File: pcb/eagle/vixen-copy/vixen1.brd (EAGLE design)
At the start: 89.6 x 59.5 mm, 33 parts, among them CN1 EXPANSIONPORT-VIC20-EDGEEDGE, IC1 74HCT393N, IC2 74AC157N, IC3 74AC157N, IC4 74AC157N, IC5 74AC157N, IC6 74ALS11N, IC8 74132N, IC9 74LS00N, U1 TMS4416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

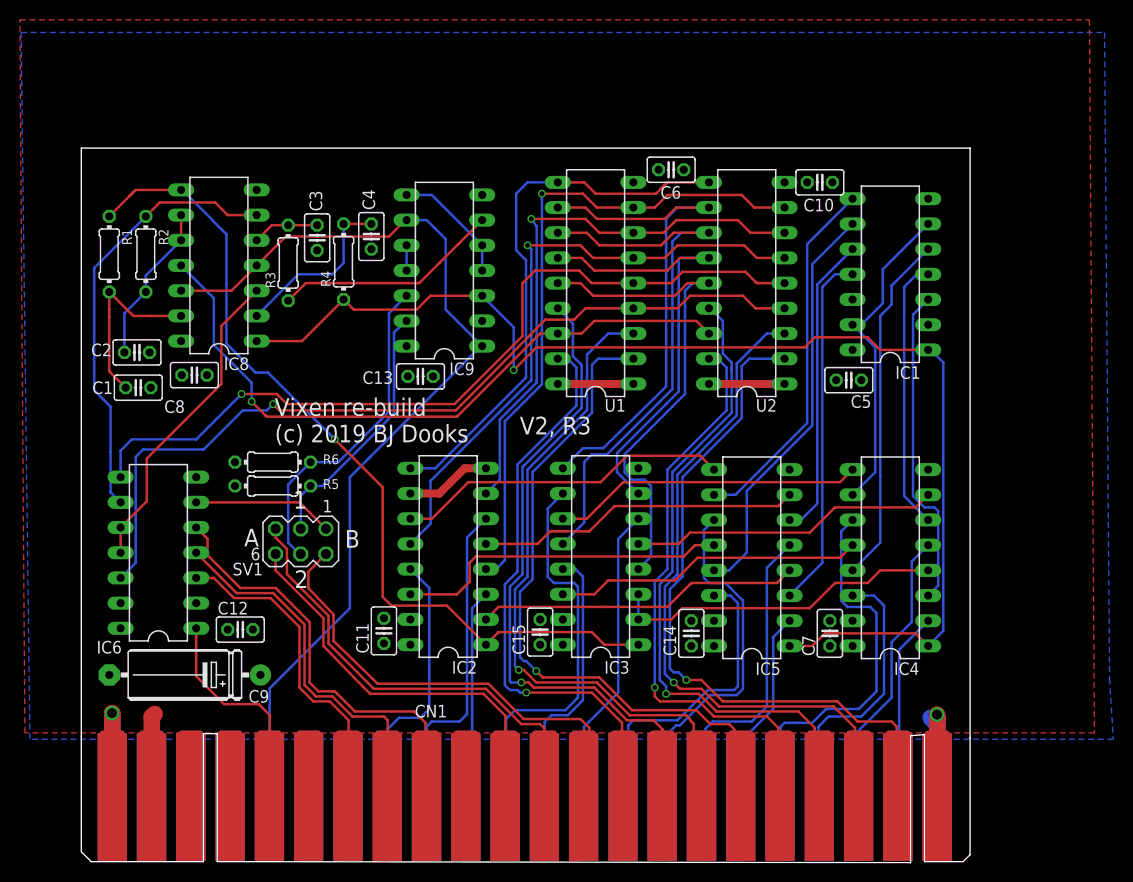
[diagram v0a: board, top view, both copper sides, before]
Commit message: vixen: minor pcb updates for v2,r3
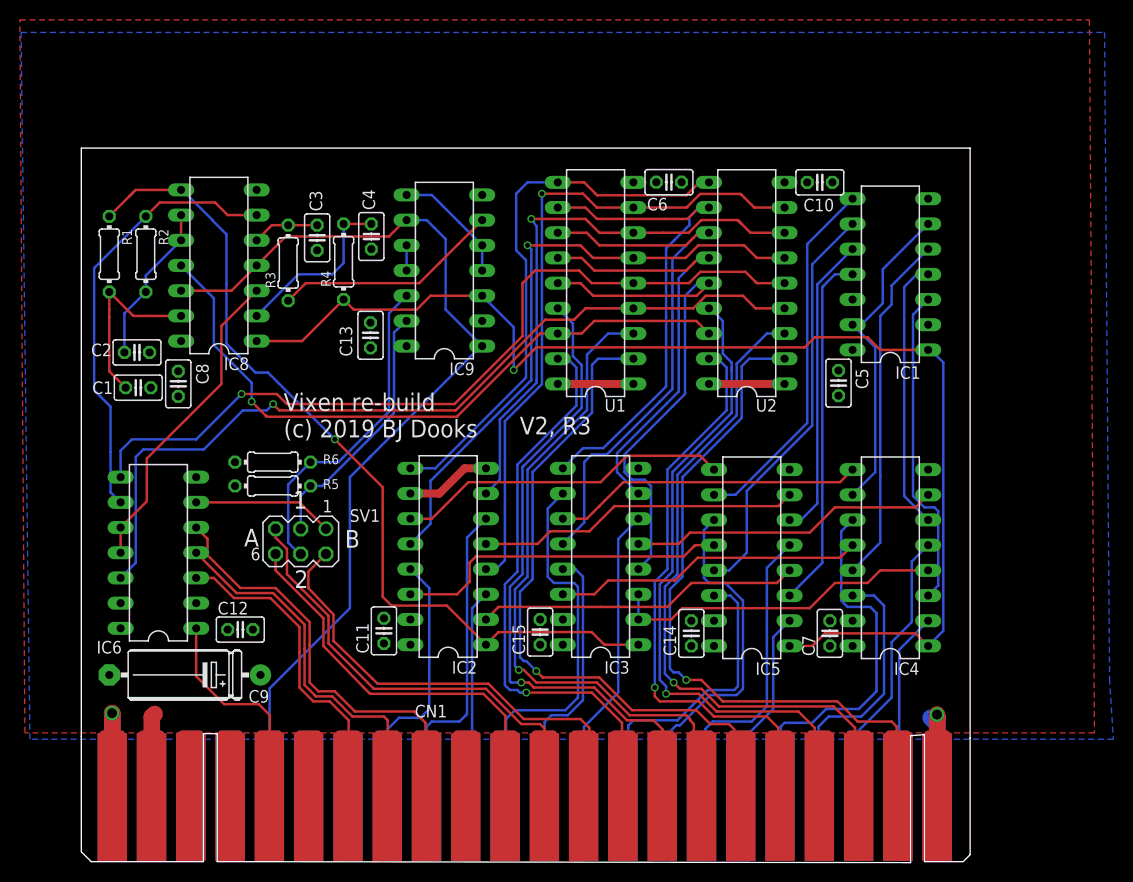
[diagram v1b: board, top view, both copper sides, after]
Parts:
- moved C13 6.52 mm to (34.0, 53.3), turned to 90 degrees
- moved C8 1.85 mm to (14.6, 48.4), turned to 270 degrees
- moved C6 1.27 mm to (64.0, 68.7), turned to 0 degrees
- moved C5 1.08 mm to (81.1, 48.5), turned to 270 degrees
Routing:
- net RA3: track 51.7 -> 50.4 mm
- net RA1: track 46.5 -> 45.4 mm
- net RA2: track 56.3 -> 55.3 mm
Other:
- board text added: "V2, R3 6 Mayl 2021"
- board text removed: "V2, R3 22 April 2021"
